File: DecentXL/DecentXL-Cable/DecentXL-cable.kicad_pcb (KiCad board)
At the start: 2 copper layers, 60.5 x 67.3 mm, 2 parts, among them J1 Conn_01x24, J2 Conn_01x26

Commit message: DecentXL cable rev 1.1
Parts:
- moved J1 86.5 mm to (20.7, 134.4)
- moved J2 70.8 mm to (55.6, 13.6)
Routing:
- net (no net): track 1764.6 -> 3003.0 mm
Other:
- board size 60.5 x 67.3 mm -> 63.5 x 118.1 mm

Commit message: DecentXL 1.1 WIP
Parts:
- moved J2 10.0 mm to (55.6, 23.6)
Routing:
- net (no net): track 3003.0 -> 2764.5 mm
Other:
- board size 63.5 x 118.1 mm -> 63.5 x 108.1 mm
- board text added: "Decent Cable (c) 2023 B. Le Roy"
- board text removed: "DecentXL cable (c) 2023 B. Le Roy"

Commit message: DecentXL revisions
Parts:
- moved J2 15.6 mm to (55.6, 39.1)
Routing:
- net (no net): track 2764.5 -> 2386.5 mm
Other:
- board size 63.5 x 108.1 mm -> 63.5 x 92.6 mm

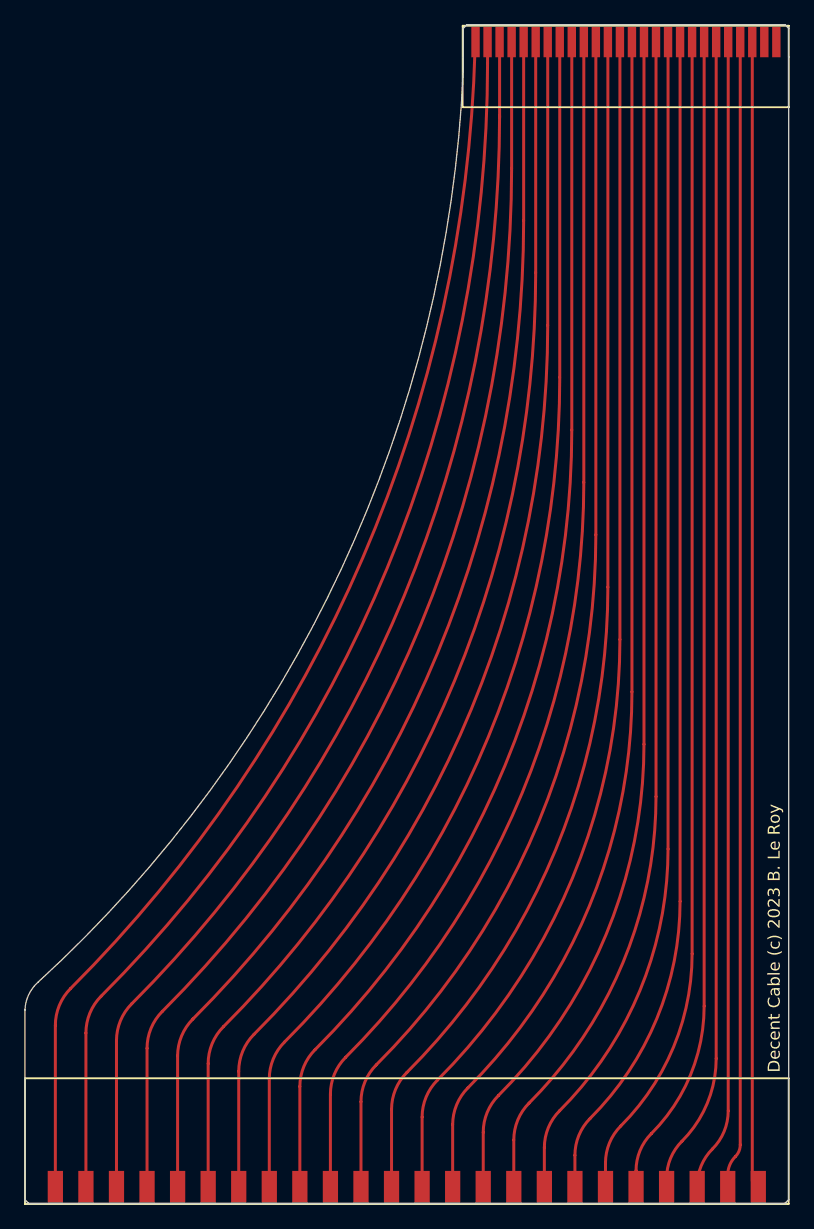
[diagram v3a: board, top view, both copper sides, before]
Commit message: Cable rev. 2
Longer contacts on the Atari side
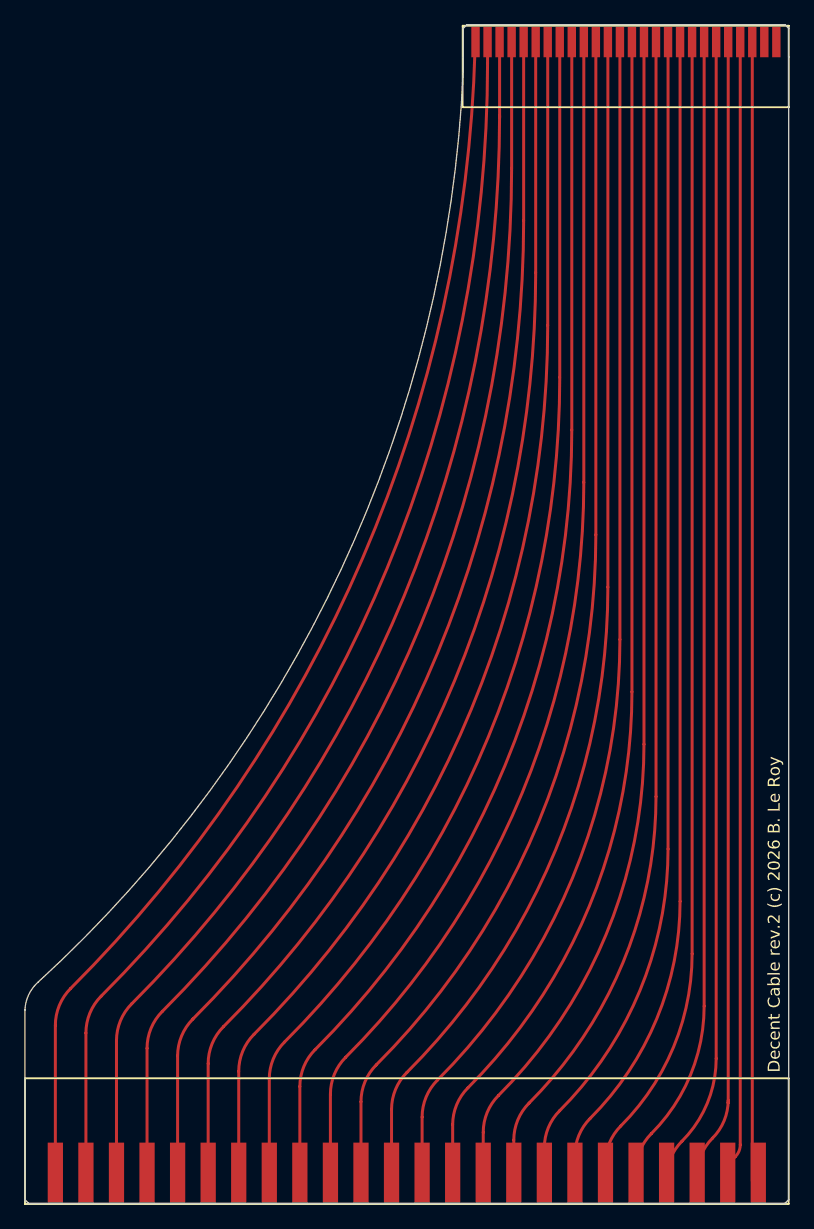
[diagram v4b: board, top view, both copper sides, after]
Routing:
- net (no net): track 2386.5 -> 2385.8 mm
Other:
- board text added: "Decent Cable rev.2 (c) 2026 B. Le Roy"
- board text removed: "Decent Cable (c) 2023 B. Le Roy"

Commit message: Decent cable rev. 2
Longer contacts on the Atari side
Teardrops
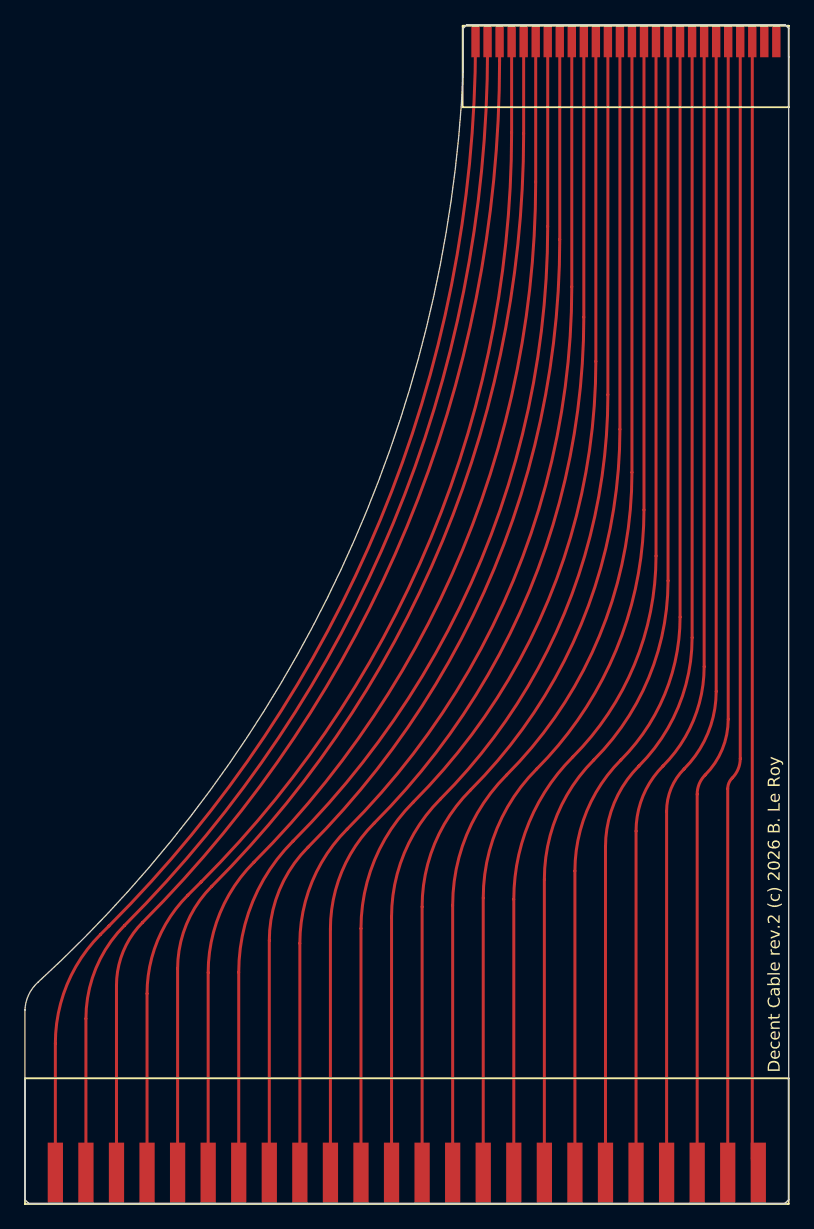
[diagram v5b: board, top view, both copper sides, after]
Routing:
- net (no net): track 2385.8 -> 2361.1 mm
